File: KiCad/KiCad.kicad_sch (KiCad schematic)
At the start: 119 parts, among them IC2 MCP23017-E_SO, IC3 MCP23017-E_SO, J1 Screw_Terminal_01x03, J10 Screw_Terminal_01x02, J11 Screw_Terminal_01x02, J12 Screw_Terminal_01x02, J13 Screw_Terminal_01x02, J14 Screw_Terminal_01x02, J15 Screw_Terminal_01x02, J16 Screw_Terminal_01x02, J18 Screw_Terminal_01x04, J2 Screw_Terminal_01x03, J3 Screw_Terminal_01x03, J4 Screw_Terminal_01x02, J5 Screw_Terminal_01x02, J6 Screw_Terminal_01x03, J7 Screw_Terminal_01x02, J8 Screw_Terminal_01x03, J9 Screw_Terminal_01x02, Q1 2N3906, Q10 2N3904, Q2 2N3906, Q3 2N3906, Q4 2N3904, Q5 2N3904, Q6 2N3904, Q7 2N3906, Q8 2N3904, Q9 2N3906, U1 L298HN, U2 L298HN, U3 L7805, U4 ARDUINO_MKR_WAN_1310, U5 L298HN, U6 L298HN, U7 LM75AIMX_NOPB

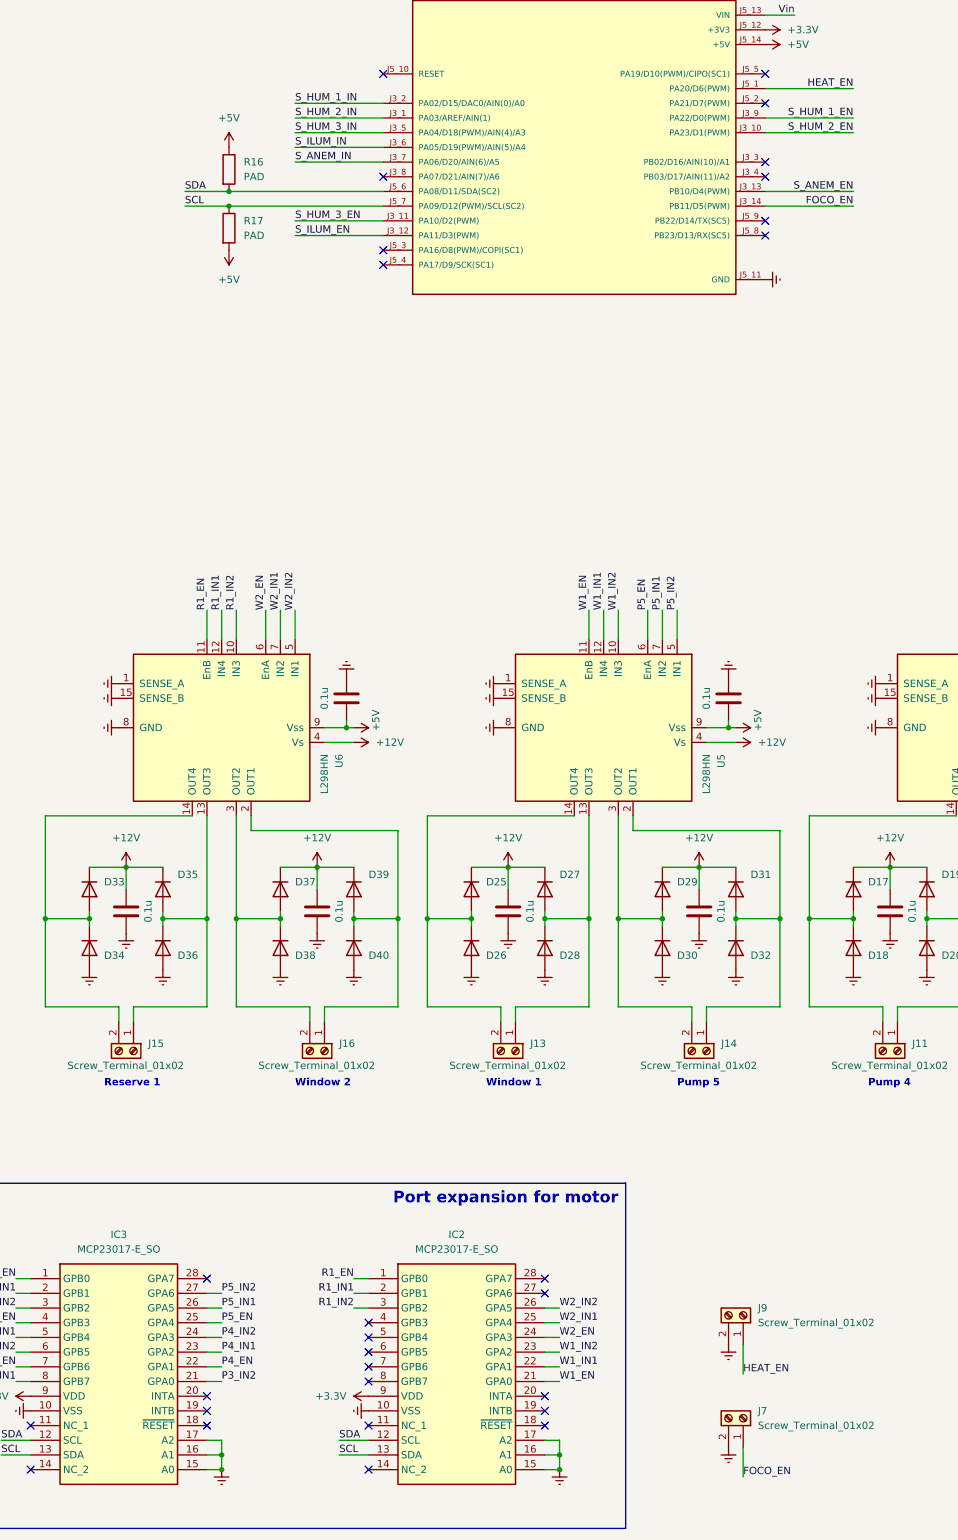
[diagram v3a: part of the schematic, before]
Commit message: addded Arduino files with definitions
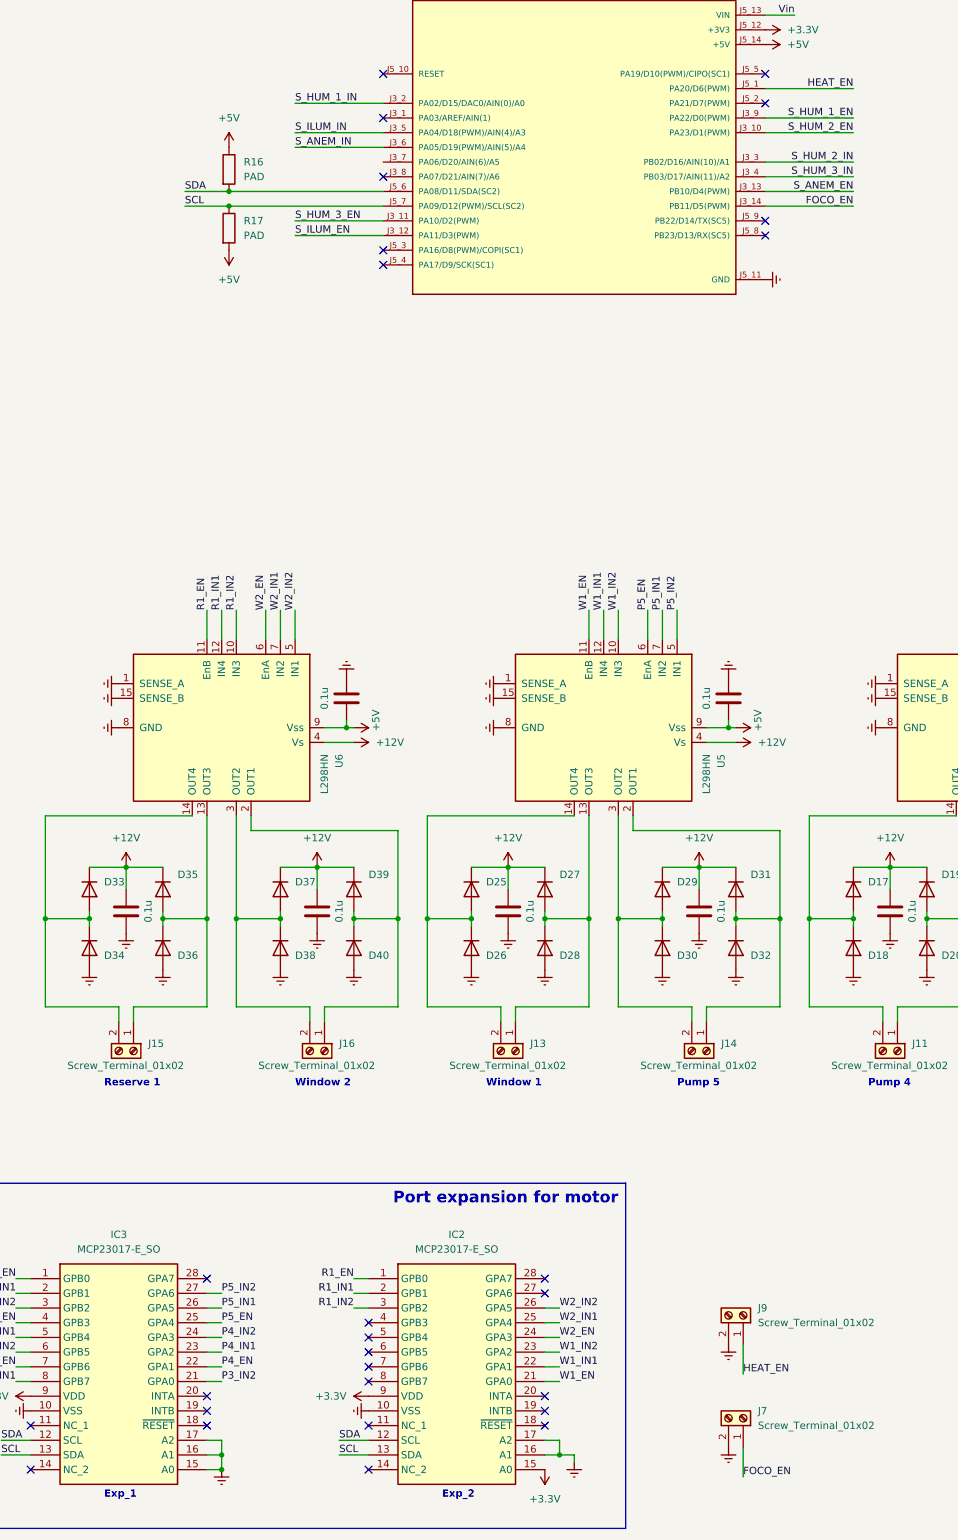
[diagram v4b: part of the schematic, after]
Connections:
- net +3.3V: now also IC2.15 (A0)
- net Earth: no longer IC2.15 (A0)
- net S_ANEM_IN: now also U4.J3_6 (PA05/D19(PWM)/AIN(5)/A4); no longer U4.J3_7 (PA06/D20/AIN(6)/A5)
- net S_HUM_2_IN: now also U4.J3_3 (PB02/D16/AIN(10)/A1); no longer U4.J3_1 (PA03/AREF/AIN(1))
- net S_HUM_3_IN: now also U4.J3_4 (PB03/D17/AIN(11)/A2); no longer U4.J3_5 (PA04/D18(PWM)/AIN(4)/A3)
- net S_ILUM_IN: now also U4.J3_5 (PA04/D18(PWM)/AIN(4)/A3); no longer U4.J3_6 (PA05/D19(PWM)/AIN(5)/A4)
- no-connect marks 29 -> 28
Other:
- note added: "Exp_1"
- note added: "Exp_2"
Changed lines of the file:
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@@
   (junction (at 138.43 179.07) (diameter 0) (color 0 0 0 0)
   )
-  (junction (at 207.01 274.32) (diameter 0) (color 0 0 0 0)
-  )
   (junction (at 149.86 55.88) (diameter 0) (color 0 0 0 0)
   )
@@
   )
   (no_connect (at 176.53 63.5))
-  (no_connect (at 242.57 48.26))
   (no_connect (at 176.53 33.02))
   (no_connect (at 204.47 241.3))
@@
   (no_connect (at 242.57 58.42))
   (no_connect (at 115.57 266.7))
-  (no_connect (at 242.57 50.8))
+  (no_connect (at 176.53 40.64))
   (no_connect (at 370.84 71.12))
   (no_connect (at 115.57 274.32))
@@
     (stroke (width 0) (type default))
   )
-  (wire (pts (xy 204.47 274.32) (xy 207.01 274.32))
-    (stroke (width 0) (type default))
-  )
   (wire (pts (xy 171.45 243.84) (xy 173.99 243.84))
     (stroke (width 0) (type default))
@@
     (stroke (width 0) (type default))
   )
-  (wire (pts (xy 207.01 271.78) (xy 207.01 274.32))
+  (wire (pts (xy 209.55 271.78) (xy 209.55 273.05))
     (stroke (width 0) (type default))
   )
@@
     (stroke (width 0) (type default))
   )
-  (wire (pts (xy 176.53 45.72) (xy 161.29 45.72))
+  (wire (pts (xy 176.53 43.18) (xy 161.29 43.18))
     (stroke (width 0) (type default))
   )
@@
     (stroke (width 0) (type default))
   )
-  (wire (pts (xy 176.53 48.26) (xy 161.29 48.26))
+  (wire (pts (xy 176.53 45.72) (xy 161.29 45.72))
     (stroke (width 0) (type default))
   )
@@
     (stroke (width 0) (type default))
   )
+  (wire (pts (xy 209.55 271.78) (xy 207.01 271.78))
+    (stroke (width 0) (type default))
+  )
   (wire (pts (xy 132.08 170.18) (xy 138.43 170.18))
     (stroke (width 0) (type default))
@@
     (stroke (width 0) (type default))
   )
+  (wire (pts (xy 242.57 50.8) (xy 257.81 50.8))
+    (stroke (width 0) (type default))
+  )
   (wire (pts (xy 59.69 86.36) (xy 59.69 88.9))
     (stroke (width 0) (type default))
@@
     (stroke (width 0) (type default))
   )
-  (wire (pts (xy 176.53 40.64) (xy 161.29 40.64))
-    (stroke (width 0) (type default))
-  )
   (wire (pts (xy 113.03 254) (xy 115.57 254))
     (stroke (width 0) (type default))
@@
     (stroke (width 0) (type default))
   )
-  (wire (pts (xy 176.53 43.18) (xy 161.29 43.18))
-    (stroke (width 0) (type default))
-  )
   (wire (pts (xy 236.22 144.78) (xy 236.22 146.05))
     (stroke (width 0) (type default))
@@
     (stroke (width 0) (type default))
   )
+  (wire (pts (xy 242.57 48.26) (xy 257.81 48.26))
+    (stroke (width 0) (type default))
+  )
   (wire (pts (xy 74.93 38.1) (xy 77.47 38.1))
     (stroke (width 0) (type default))
@@
     (effects (font (size 1.27 1.27) (thickness 0.254) bold) (justify left bottom))
   )
+  (text "Exp_2" (at 186.69 279.4 0)
+    (effects (font (size 1.27 1.27) (thickness 0.254) bold) (justify left bottom))
+  )
   (text "Pump 2" (at 325.12 208.28 0)
     (effects (font (size 1.27 1.27) (thickness 0.254) bold) (justify left bottom))
   )
+  (text "Exp_1" (at 128.27 279.4 0)
+    (effects (font (size 1.27 1.27) (thickness 0.254) bold) (justify left bottom))
+  )
   (text "Power\n" (at 403.86 17.78 0)
     (effects (font (size 2 2) (thickness 0.4) bold) (justify right bottom))
@@
     (effects (font (size 1.27 1.27)) (justify left bottom))
   )
+  (label "S_HUM_2_IN" (at 257.81 48.26 180) (fields_autoplaced)
+    (effects (font (size 1.27 1.27)) (justify right bottom))
+  )
   (label "W2_IN1" (at 158.75 125.73 90) (fields_autoplaced)
     (effects (font (size 1.27 1.27)) (justify left bottom))
@@
     (effects (font (size 1.27 1.27)) (justify left bottom))
   )
-  (label "S_HUM_2_IN" (at 161.29 40.64 0) (fields_autoplaced)
-    (effects (font (size 1.27 1.27)) (justify left bottom))
-  )
   (label "S_HUM_1_IN" (at 161.29 38.1 0) (fields_autoplaced)
     (effects (font (size 1.27 1.27)) (justify left bottom))
@@
     (effects (font (size 1.27 1.27)) (justify left bottom))
   )
-  (label "S_HUM_3_IN" (at 161.29 43.18 0) (fields_autoplaced)
-    (effects (font (size 1.27 1.27)) (justify left bottom))
-  )
   (label "W2_EN" (at 207.01 251.46 0) (fields_autoplaced)
     (effects (font (size 1.27 1.27)) (justify left bottom))
@@
     (effects (font (size 1.27 1.27)) (justify left bottom))
   )
+  (label "S_HUM_3_IN" (at 257.81 50.8 180) (fields_autoplaced)
+    (effects (font (size 1.27 1.27)) (justify right bottom))
+  )
   (label "P5_IN2" (at 227.33 125.73 90) (fields_autoplaced)
     (effects (font (size 1.27 1.27)) (justify left bottom))
@@
     (effects (font (size 1.27 1.27)) (justify right bottom))
   )
-  (label "S_ANEM_IN" (at 161.29 48.26 0) (fields_autoplaced)
+  (label "S_ANEM_IN" (at 161.29 45.72 0) (fields_autoplaced)
     (effects (font (size 1.27 1.27)) (justify left bottom))
   )
@@
     (effects (font (size 1.27 1.27)) (justify right bottom))
   )
-  (label "S_ILUM_IN" (at 161.29 45.72 0) (fields_autoplaced)
+  (label "S_ILUM_IN" (at 161.29 43.18 0) (fields_autoplaced)
     (effects (font (size 1.27 1.27)) (justify left bottom))
   )
@@
     )
   )
-  (symbol (lib_name "Earth_2") (lib_id "power:Earth") (at 207.01 274.32 0) (unit 1)
+  (symbol (lib_name "Earth_2") (lib_id "power:Earth") (at 209.55 273.05 0) (unit 1)
     (in_bom yes) (on_board yes) (dnp no) (fields_autoplaced)
-    (property "Reference" "#PWR0113" (at 207.01 280.67 0)
+    (property "Reference" "#PWR0113" (at 209.55 279.4 0)
       (effects (font (size 1.27 1.27)) hide)
     )
-    (property "Value" "Earth" (at 207.01 278.13 0)
+    (property "Value" "Earth" (at 209.55 276.86 0)
       (effects (font (size 1.27 1.27)) hide)
     )
-    (property "Footprint" "" (at 207.01 274.32 0)
+    (property "Footprint" "" (at 209.55 273.05 0)
       (effects (font (size 1.27 1.27)) hide)
     )
-    (property "Datasheet" "~" (at 207.01 274.32 0)
+    (property "Datasheet" "~" (at 209.55 273.05 0)
       (effects (font (size 1.27 1.27)) hide)
     )
@@
         )
       )
+    )
+  )
+  (symbol (lib_name "+3.3V_1") (lib_id "power:+3.3V") (at 204.47 274.32 180) (unit 1)
+    (in_bom yes) (on_board yes) (dnp no) (fields_autoplaced)
+    (property "Reference" "#PWR0114" (at 204.47 270.51 0)
+      (effects (font (size 1.27 1.27)) hide)
+    )
+    (property "Value" "+3.3V" (at 204.47 279.4 0)
+      (effects (font (size 1.27 1.27)))
+    )
+    (property "Footprint" "" (at 204.47 274.32 0)
+      (effects (font (size 1.27 1.27)) hide)
+    )
+    (property "Datasheet" "" (at 204.47 274.32 0)
+      (effects (font (size 1.27 1.27)) hide)
+    )
+    (pin "1")
+    (instances
+      (project "KiCad"
+        (path "/557850ac-a946-4dff-8187-8978353577df"
+          (reference "#PWR0114") (unit 1)
+        )
+      )

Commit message: defines
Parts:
- removed J7: Screw_Terminal_01x02, TerminalBlock_Phoenix:TerminalBlock_Phoenix_MKDS-1,5-2_1x02_P5.00mm_Horizontal, symbol Connector:Screw_Terminal_01x02
- added C15: 0.1u, Capacitor_SMD:C_1206_3216Metric_Pad1.33x1.80mm_HandSolder, symbol Device:C
- added J12: Screw_Terminal_01x05, symbol Connector:Screw_Terminal_01x05
- renumbered C12 to C1, C2 to C10, C5 to C11, C1 to C12, C3 to C13, C4 to C14, C13 to C2, C14 to C3, C9 to C4, C10 to C5, C11 to C6, C6 to C7, C7 to C8, C8 to C9, D42 to D10, D33 to D11, D34 to D12, D35 to D13, D36 to D14, D37 to D15, D38 to D16, D39 to D17, D40 to D18, D25 to D19, D26 to D20, D27 to D21, D28 to D22, D29 to D23, D30 to D24, D31 to D25, D32 to D26, D17 to D27, D18 to D28, D19 to D29, D20 to D30, D21 to D31, D22 to D32, D23 to D33, D24 to D34, D7 to D35, D8 to D36, D9 to D37, D10 to D38, D13 to D39, D14 to D40, D15 to D41, D16 to D42, D11 to D7, D12 to D8, D41 to D9, IC3 to IC1, J9 to J10, J12 to J13, J4 to J14, J10 to J15, J5 to J16, J18 to J17, J6 to J4, J8 to J5, J15 to J6, J16 to J7, J13 to J8, J14 to J9, Q7 to Q4, Q9 to Q5, Q4 to Q6, Q5 to Q7, Q6 to Q8, Q8 to Q9, R24 to R10, R7 to R11, R8 to R12, R9 to R13, R20 to R14, R25 to R15, R10 to R16, R11 to R17, R12 to R18, R21 to R19, R26 to R20, R13 to R21, R14 to R22, R15 to R23, R22 to R24, R27 to R25, R16 to R26, R17 to R27, R18 to R7, R19 to R8, R23 to R9, U6 to U1, U4 to U2, U5 to U3, U1 to U4, U2 to U5, U7 to U6, U3 to U7
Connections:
- net FOCO_EN is gone; now on net HEAT_EN: U2.J3_14 (PB11/D5(PWM))
- net +5V: now also C15.1
- net Earth: now also C15.2, J12.5 (Pin_5)
- net HEAT_EN: no longer U2.J5_1 (PA20/D6(PWM))
- net FOCO2_EN: now reaches U2.J5_2 (PA21/D7(PWM))
- net FOCO2_EN: now also J12.2 (Pin_2)
- net FOCO3_EN: now reaches U2.J5_3 (PA16/D8(PWM)/COPI(SC1))
- net FOCO3_EN: now also J12.3 (Pin_3)
- net FOCO4_EN: now reaches U2.J5_4 (PA17/D9/SCK(SC1))
- net FOCO4_EN: now also J12.4 (Pin_4)
- new net FOCO1_EN: J12.1 (Pin_1), U2.J5_1 (PA20/D6(PWM))
- no-connect marks 28 -> 25
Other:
- moved on the sheet: J10, U6

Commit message: sch done
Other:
- moved on the sheet: J10, J12
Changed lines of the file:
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@@
     (stroke (width 0) (type default))
   )
-  (wire (pts (xy 234.95 273.05) (xy 234.95 278.13))
+  (wire (pts (xy 392.43 196.85) (xy 392.43 201.93))
     (stroke (width 0) (type default))
   )
@@
     (stroke (width 0) (type default))
   )
-  (wire (pts (xy 261.62 270.51) (xy 261.62 267.97))
+  (wire (pts (xy 388.62 168.91) (xy 388.62 166.37))
     (stroke (width 0) (type default))
   )
@@
     (stroke (width 0) (type default))
   )
-  (wire (pts (xy 269.24 270.51) (xy 269.24 267.97))
+  (wire (pts (xy 396.24 168.91) (xy 396.24 166.37))
     (stroke (width 0) (type default))
   )
@@
     (stroke (width 0) (type default))
   )
-  (wire (pts (xy 266.7 270.51) (xy 266.7 267.97))
+  (wire (pts (xy 393.7 168.91) (xy 393.7 166.37))
     (stroke (width 0) (type default))
   )
@@
     (stroke (width 0) (type default))
   )
-  (wire (pts (xy 264.16 270.51) (xy 264.16 267.97))
+  (wire (pts (xy 391.16 168.91) (xy 391.16 166.37))
     (stroke (width 0) (type default))
   )
@@
     (fill (type none))
   )
-  (text_box "FALTA LO DE LA ILUMINACION\n"
-    (at 278.13 48.26 0) (size 74.93 40.64)
-    (stroke (width 0) (type default))
-    (fill (type none))
-    (effects (font (size 7 7) (thickness 1.4) bold) (justify left top))
-  )
   (text "Sensor\ncond.\n\n" (at 90.17 22.86 0)
     (effects (font (size 2 2) (thickness 0.4) bold) (justify right bottom))
@@
     (effects (font (size 1.27 1.27)) (justify left bottom))
   )
-  (label "FOCO2_EN" (at 264.16 270.51 270) (fields_autoplaced)
+  (label "FOCO2_EN" (at 391.16 168.91 270) (fields_autoplaced)
     (effects (font (size 1.27 1.27)) (justify right bottom))
   )
@@
     (effects (font (size 1.27 1.27)) (justify left bottom))
   )
-  (label "HEAT_EN" (at 234.95 278.13 180) (fields_autoplaced)
+  (label "HEAT_EN" (at 392.43 201.93 180) (fields_autoplaced)
     (effects (font (size 1.27 1.27)) (justify right bottom))
   )
@@
     (effects (font (size 1.27 1.27)) (justify left bottom))
   )
-  (label "FOCO3_EN" (at 266.7 270.51 270) (fields_autoplaced)
+  (label "FOCO3_EN" (at 393.7 168.91 270) (fields_autoplaced)
     (effects (font (size 1.27 1.27)) (justify right bottom))
   )
@@
     (effects (font (size 1.27 1.27)) (justify left bottom))
   )
-  (label "FOCO1_EN" (at 261.62 270.51 270) (fields_autoplaced)
+  (label "FOCO1_EN" (at 388.62 168.91 270) (fields_autoplaced)
     (effects (font (size 1.27 1.27)) (justify right bottom))
   )
@@
     (effects (font (size 1.27 1.27)) (justify left bottom))
   )
-  (label "FOCO4_EN" (at 269.24 270.51 270) (fields_autoplaced)
+  (label "FOCO4_EN" (at 396.24 168.91 270) (fields_autoplaced)
     (effects (font (size 1.27 1.27)) (justify right bottom))
   )
@@
     )
   )
-  (symbol (lib_name "Earth_1") (lib_id "power:Earth") (at 271.78 267.97 0) (unit 1)
+  (symbol (lib_name "Earth_1") (lib_id "power:Earth") (at 398.78 166.37 0) (unit 1)
     (in_bom yes) (on_board yes) (dnp no) (fields_autoplaced)
-    (property "Reference" "#PWR084" (at 271.78 274.32 0)
+    (property "Reference" "#PWR084" (at 398.78 172.72 0)
       (effects (font (size 1.27 1.27)) hide)
     )
-    (property "Value" "Earth" (at 271.78 271.78 0)
+    (property "Value" "Earth" (at 398.78 170.18 0)
       (effects (font (size 1.27 1.27)) hide)
     )
-    (property "Footprint" "" (at 271.78 267.97 0)
+    (property "Footprint" "" (at 398.78 166.37 0)
       (effects (font (size 1.27 1.27)) hide)
     )
-    (property "Datasheet" "~" (at 271.78 267.97 0)
+    (property "Datasheet" "~" (at 398.78 166.37 0)
       (effects (font (size 1.27 1.27)) hide)
     )
@@
     )
   )
-  (symbol (lib_id "Connector:Screw_Terminal_01x02") (at 234.95 267.97 90) (unit 1)
+  (symbol (lib_id "Connector:Screw_Terminal_01x02") (at 392.43 191.77 90) (unit 1)
     (in_bom yes) (on_board yes) (dnp no)
-    (property "Reference" "J10" (at 237.49 265.43 90)
+    (property "Reference" "J10" (at 394.97 189.23 90)
       (effects (font (size 1.27 1.27)) (justify left))
     )
-    (property "Value" "Screw_Terminal_01x02" (at 247.65 262.89 90)
+    (property "Value" "Screw_Terminal_01x02" (at 405.13 186.69 90)
       (effects (font (size 1.27 1.27)) (justify left))
     )
-    (property "Footprint" "TerminalBlock_Phoenix:TerminalBlock_Phoenix_MKDS-1,5-2_1x02_P5.00mm_Horizontal" (at 234.95 267.97 0)
+    (property "Footprint" "TerminalBlock_Phoenix:TerminalBlock_Phoenix_MKDS-1,5-2_1x02_P5.00mm_Horizontal" (at 392.43 191.77 0)
       (effects (font (size 1.27 1.27)) hide)
     )
-    (property "Datasheet" "~" (at 234.95 267.97 0)
+    (property "Datasheet" "~" (at 392.43 191.77 0)
       (effects (font (size 1.27 1.27)) hide)
     )
@@
     )
   )
-  (symbol (lib_id "Connector:Screw_Terminal_01x05") (at 266.7 262.89 90) (unit 1)
+  (symbol (lib_id "Connector:Screw_Terminal_01x05") (at 393.7 161.29 90) (unit 1)
     (in_bom yes) (on_board yes) (dnp no)
-    (property "Reference" "J12" (at 266.7 260.35 90)
+    (property "Reference" "J12" (at 393.7 158.75 90)
       (effects (font (size 1.27 1.27)))
     )
-    (property "Value" "Screw_Terminal_01x05" (at 266.7 257.81 90)
+    (property "Value" "Screw_Terminal_01x05" (at 393.7 156.21 90)
       (effects (font (size 1.27 1.27)))
     )
-    (property "Footprint" "" (at 266.7 262.89 0)
+    (property "Footprint" "" (at 393.7 161.29 0)
       (effects (font (size 1.27 1.27)) hide)
     )
-    (property "Datasheet" "~" (at 266.7 262.89 0)
+    (property "Datasheet" "~" (at 393.7 161.29 0)
       (effects (font (size 1.27 1.27)) hide)
     )
@@
     )
   )
-  (symbol (lib_name "Earth_1") (lib_id "power:Earth") (at 237.49 273.05 0) (mirror y) (unit 1)
+  (symbol (lib_name "Earth_1") (lib_id "power:Earth") (at 394.97 196.85 0) (mirror y) (unit 1)
     (in_bom yes) (on_board yes) (dnp no) (fields_autoplaced)
-    (property "Reference" "#PWR073" (at 237.49 279.4 0)
+    (property "Reference" "#PWR073" (at 394.97 203.2 0)
       (effects (font (size 1.27 1.27)) hide)
     )
-    (property "Value" "Earth" (at 237.49 276.86 0)
+    (property "Value" "Earth" (at 394.97 200.66 0)
       (effects (font (size 1.27 1.27)) hide)
     )
-    (property "Footprint" "" (at 237.49 273.05 0)
+    (property "Footprint" "" (at 394.97 196.85 0)
       (effects (font (size 1.27 1.27)) hide)
     )
-    (property "Datasheet" "~" (at 237.49 273.05 0)
+    (property "Datasheet" "~" (at 394.97 196.85 0)
       (effects (font (size 1.27 1.27)) hide)
     )

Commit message: kicad sch finalised
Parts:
- added J10, J12: Screw_Terminal_01x02, TerminalBlock_Phoenix:TerminalBlock_Phoenix_MKDS-1,5-2_1x02_P5.00mm_Horizontal, symbol Connector:Screw_Terminal_01x02
- added K1, K2: 2071556-9, 20715569, symbol SamacSys_Parts:2071556-9
- added Q11, Q12: 2N3904, Package_TO_SOT_SMD:SOT-23, symbol Transistor_BJT:2N3904
- added R28: 10k, Resistor_SMD:R_1206_3216Metric_Pad1.30x1.75mm_HandSolder, symbol Device:R
- added R29, R30: 1.5k, Resistor_SMD:R_1206_3216Metric_Pad1.30x1.75mm_HandSolder, symbol Device:R
- added SW1: SW_Push, Button_Switch_THT:SW_PUSH_6mm_H4.3mm, symbol Switch:SW_Push
- renumbered J12 to J11, J11 to J13, J10 to J14, J17 to J15, J13 to J16, J14 to J17, J15 to J18, J16 to J19
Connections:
- net +3.3V: now also R28.1
- net +5V: now also K1.2 (COIL_2), K2.2 (COIL_2)
- net Earth: now also Q11.1 (E), Q12.1 (E), SW1.2
- net PULSE_IN: now reaches U2.J3_7 (PA06/D20/AIN(6)/A5)
- net PULSE_IN: now also R28.2, SW1.1
- net RELAY_2_EN: now reaches IC2.27 (GPA6)
- net RELAY_2_EN: now also R29.2
- net RELAY_1_EN: now reaches IC2.28 (GPA7)
- net RELAY_1_EN: now also R30.2
- net FOCO1_EN renamed FOCO_1_EN
- net FOCO2_EN renamed FOCO_2_EN
- net FOCO3_EN renamed FOCO_3_EN
- net FOCO4_EN renamed FOCO_4_EN
- new net: Q12.2 (B), R30.1
- new net: K2.1 (COIL_1), Q12.3 (C)
- new net: Q11.2 (B), R29.1
- new net: K1.1 (COIL_1), Q11.3 (C)
- new net COM_1: J10.2 (Pin_2), K2.3 (COM)
- new net COM_2: J12.2 (Pin_2), K1.3 (COM)
- new net NO_1: J10.1 (Pin_1), K2.4 (NO)
- new net NO_2: J12.1 (Pin_1), K1.4 (NO)
- no-connect marks 25 -> 23
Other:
- note added: "Blinds control"
- note added: "External Interfacing"
- note added: "Heater"
- note added: "I2C Bus"
- note added: "Lighting"
- note added: "Manual control"
- note added: "Motor Drivers"
- note added: "Port expansion"
- note added: "Relay 1"
- note added: "Relay 2"
- note added: "Temp. Sensor"
- note removed: "Port expansion for motor"
- moved on the sheet: C15, D1, D10, D11, D12, D13, D14, D15, D16, D17, D18, D19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
